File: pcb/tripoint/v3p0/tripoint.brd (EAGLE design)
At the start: 31.8 x 27.5 mm, 65 parts, among them J2 TC2030-JLINK-NL, T1 HHM1595A1, U1 STM32F091CC, U2 DW1000, U3 SKY13317, U4 LXDC2HN18A, X1 38.4M, X2 16M

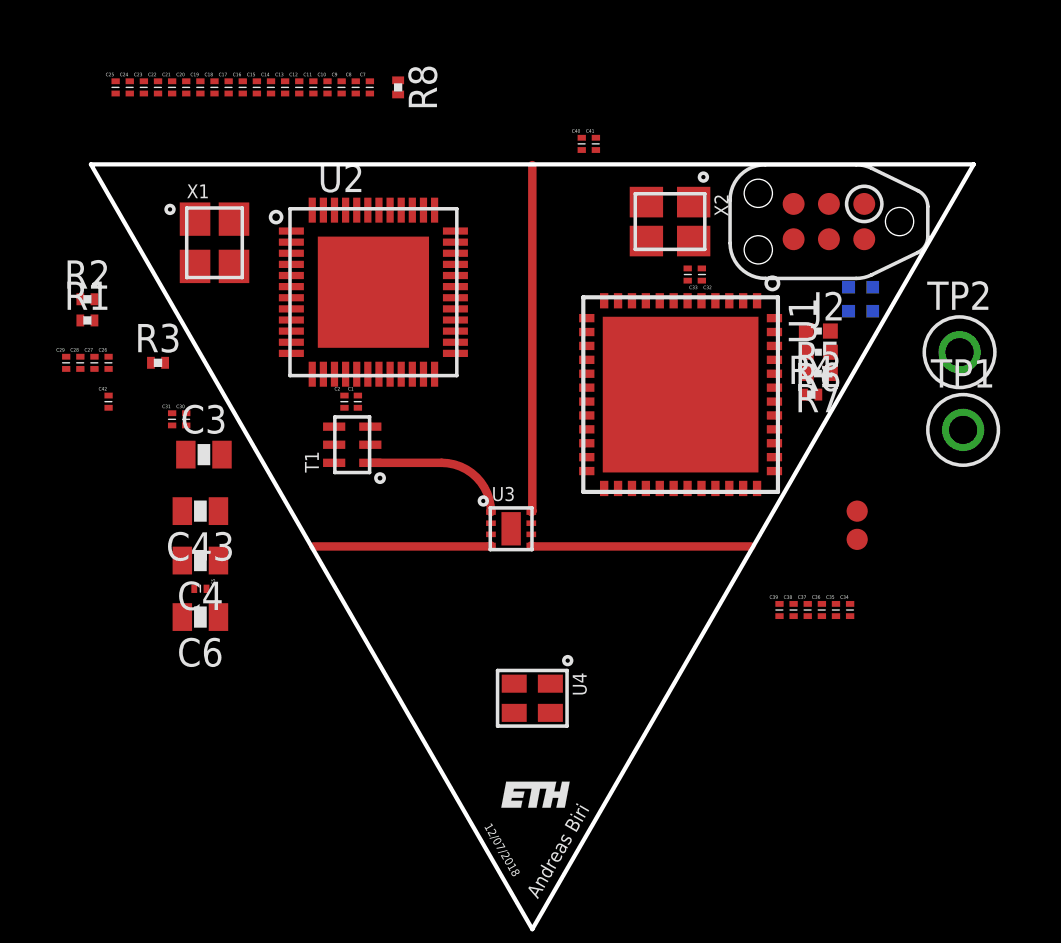
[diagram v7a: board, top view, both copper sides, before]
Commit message: completed layout, optimized pin positioning for module
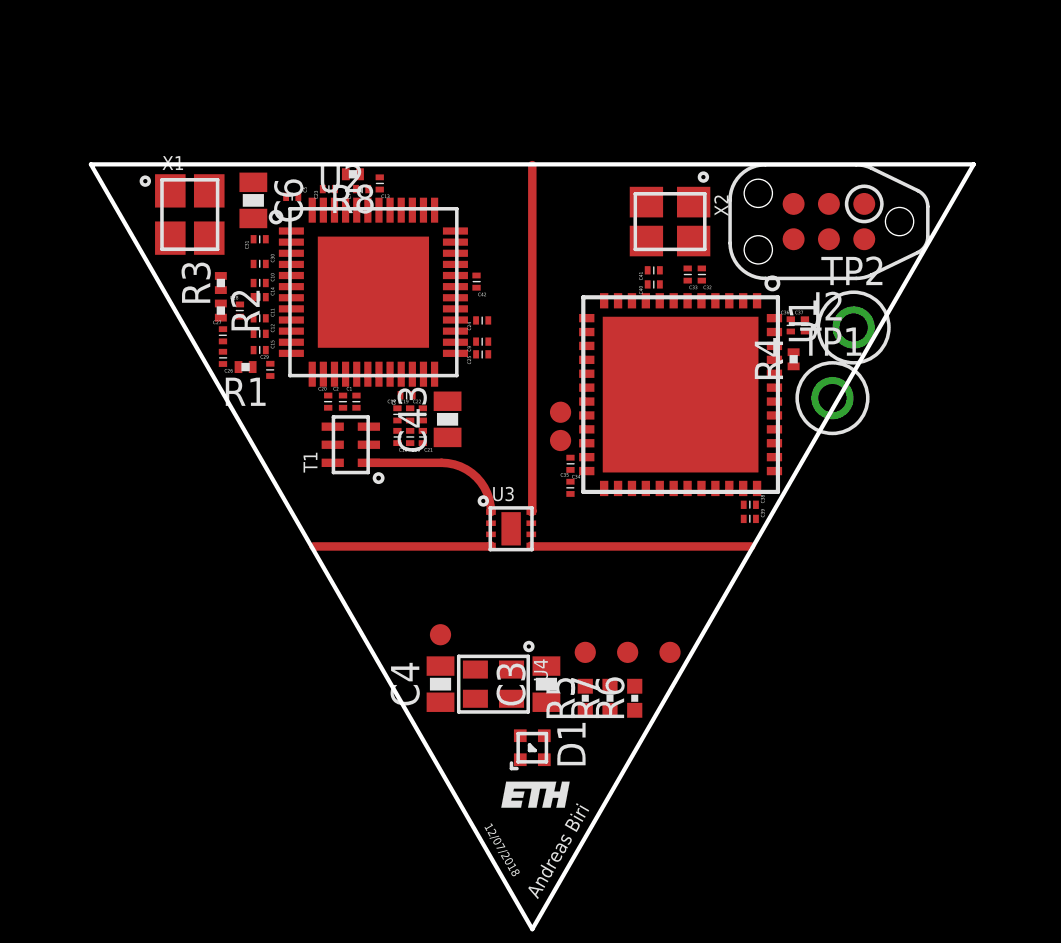
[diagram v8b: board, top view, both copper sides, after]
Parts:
- added TP5, TP6, TP7, TP8: TEST-POINT, headers:PAD.03X.03
- moved D1 20.0 mm to (0.00, -11.8), flipped to the top, turned to 180 degrees
- moved C25 16.3 mm to (-1.80, 2.34), turned to 90 degrees
- moved R5 15.6 mm to (1.91, -10.0), turned to 90 degrees
- moved C21 15.5 mm to (-3.94, -0.64), turned to 180 degrees
- moved C24 15.2 mm to (-1.80, 3.56), turned to 90 degrees
- moved C22 15.1 mm to (-3.94, 0.18)
- moved C6 15.1 mm to (-10.0, 7.87), turned to 270 degrees
- moved C3 14.8 mm to (0.51, -9.53), turned to 90 degrees
- moved C5 14.5 mm to (-8.64, 8.00)
- moved C18 14.4 mm to (-4.39, -0.64), turned to 180 degrees
- moved R6 14.1 mm to (3.68, -10.0), turned to 90 degrees
- moved C19 14.0 mm to (-4.39, 0.18)
- moved C42 13.9 mm to (-2.01, 4.95), turned to 180 degrees
- moved R7 13.9 mm to (2.79, -10.0), turned to 90 degrees
- moved C16 13.7 mm to (-4.85, -0.64), turned to 180 degrees
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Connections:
- net ANT_SEL1: now also U1.27; no longer U1.39
- net ANT_SEL2: now also U1.26; no longer U1.40
- net ANT_SEL3: now also U1.25; no longer U1.41
- net GND: now also TP8.P$1
- net LED_BLUE: now also TP6.P$1, U1.40; no longer U1.25
- net LED_GREEN: now also TP5.P$1, U1.39; no longer U1.26
- net LED_RED: now also TP7.P$1, U1.41; no longer U1.27
